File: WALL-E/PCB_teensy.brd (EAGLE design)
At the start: 92.8 x 120.8 mm, 43 parts, among them U4 R-78E5.0-0.5

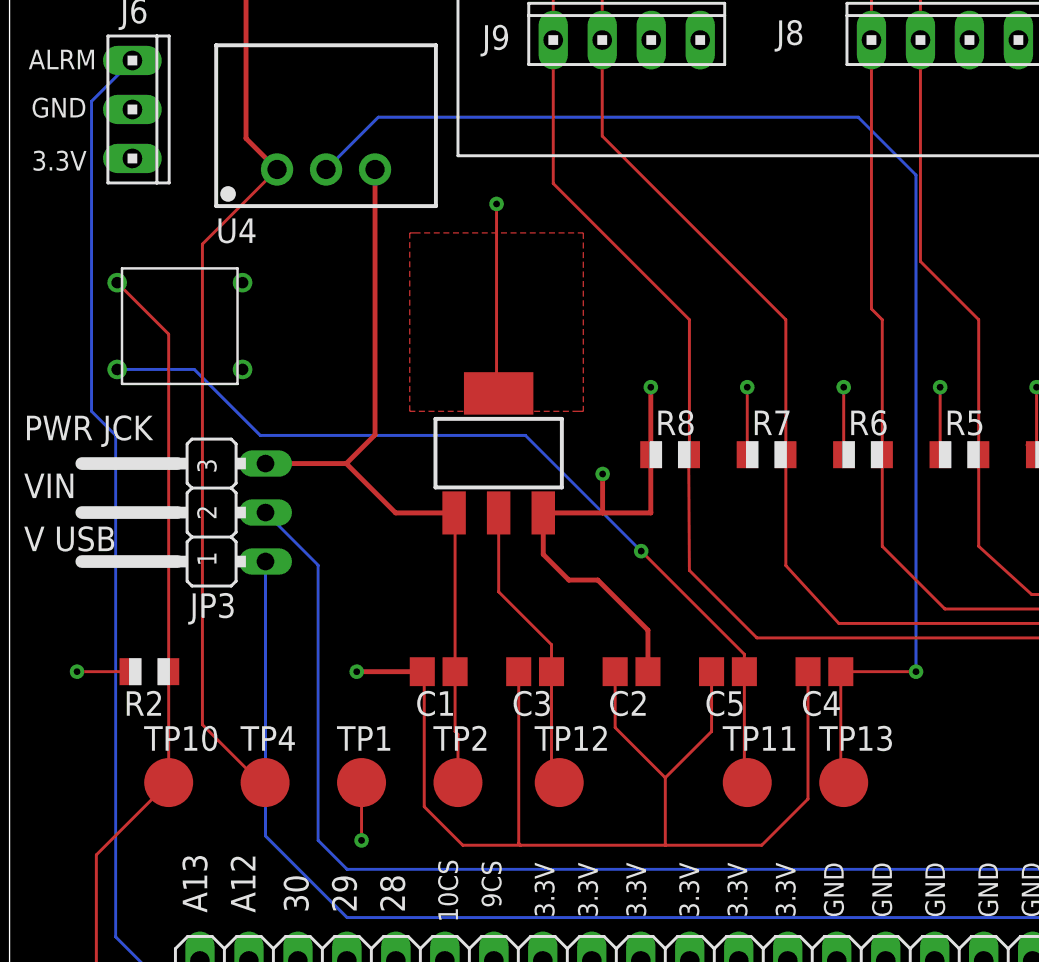
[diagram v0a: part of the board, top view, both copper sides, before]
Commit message: removed some unneeded bypass caps
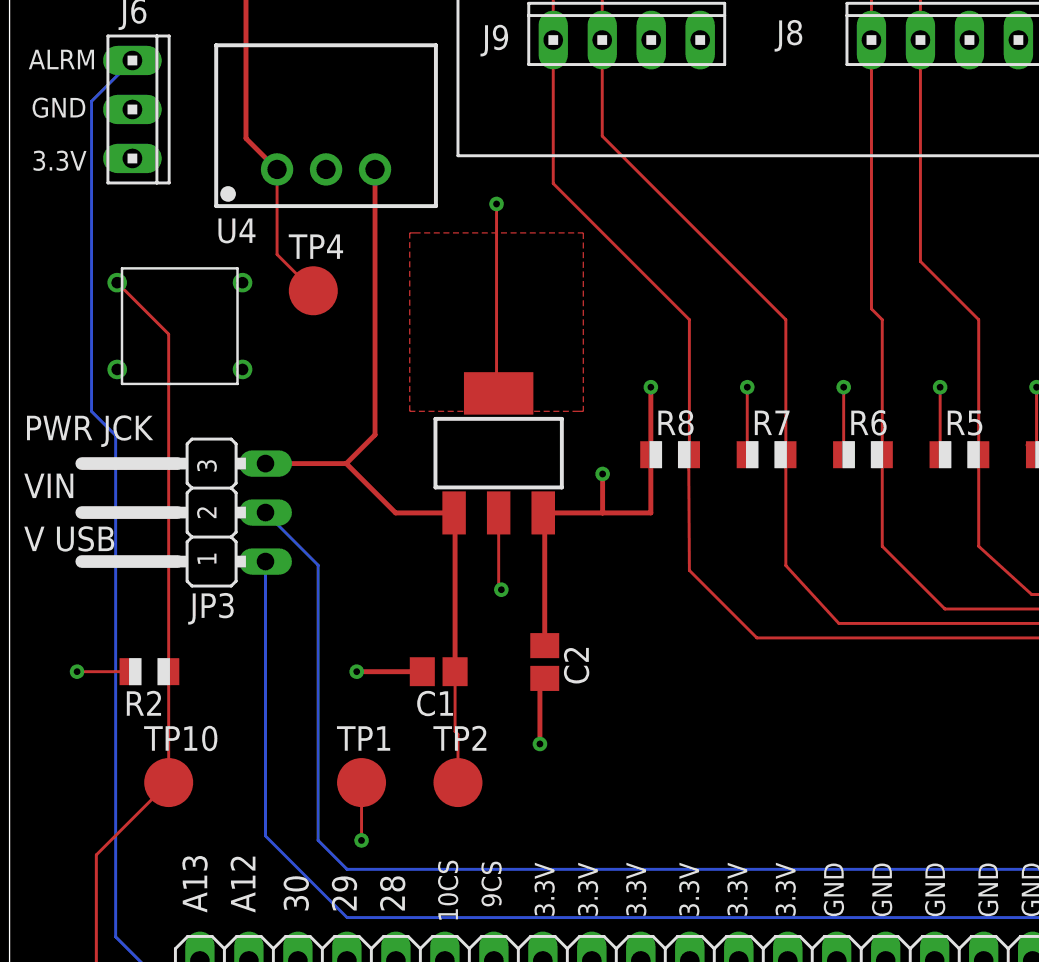
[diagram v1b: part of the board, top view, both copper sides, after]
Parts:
- removed C3, C4, C5: (no value), adafruit:C0805
- removed TP11, TP12, TP13: PTR1B2,54, testpad:B2,54
- moved TP4 25.6 mm to (15.8, 71.0)
- moved C2 4.53 mm to (27.8, 51.8), turned to 270 degrees
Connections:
- removed net N$1: C4.1, TP13.TP, U4.2
- removed net N$3: C3.1, TP12.TP, U$5.2
- removed net N$5: C5.1, TP11.TP, U$2.P$3
- net GND: now also U$2.P$3, U$5.2, U4.2; no longer C3.2, C4.2, C5.2
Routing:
- net N$1: track 68.5 -> 0.00 mm, vias 1 -> 0
- net GND: track 76.2 -> 22.9 mm, vias 3 -> 5
- net N$5: track 45.4 -> 0.00 mm, vias 1 -> 0
- net +12V: track 66.1 -> 38.3 mm
- net N$3: track 15.4 -> 0.00 mm
- net 3.3V: track 49.4 -> 45.0 mm

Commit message: generated new gerber and drill files
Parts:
- moved C1 17.6 mm to (16.2, 67.8)
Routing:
- net 5V: track 40.9 -> 43.0 mm
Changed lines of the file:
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@@
 </autorouter>
 <elements>
-<element name="C1" library="adafruit" library_urn="urn:adsk.eagle:library:420" package="C0805" value="" x="22.25" y="51.25" rot="R180"/>
+<element name="C1" library="adafruit" library_urn="urn:adsk.eagle:library:420" package="C0805" value="" x="16.25" y="67.75" smashed="yes" rot="R180">
+<attribute name="NAME" x="18.139" y="66.234" size="1.27" layer="25" rot="R180"/>
+<attribute name="VALUE" x="17.139" y="70.036" size="1.27" layer="27" rot="R180"/>
+</element>
 <element name="C2" library="adafruit" library_urn="urn:adsk.eagle:library:420" package="C0805" value="" x="27.75" y="51.75" rot="R270"/>
 <element name="J1" library="con-amp" library_urn="urn:adsk.eagle:library:127" package="10X04MTA" value="" x="86.75" y="103.75" smashed="yes" rot="R90">
@@
 <wire x1="25.25" y1="65.789" x2="25.25" y2="75.5" width="0.1524" layer="1"/>
 <via x="25.25" y="75.5" extent="1-16" drill="0.35"/>
-<wire x1="21.5" y1="51.15" x2="21.4" y2="51.25" width="0.1524" layer="1"/>
-<wire x1="21.4" y1="51.25" x2="18" y2="51.25" width="0.254" layer="1"/>
-<via x="18" y="51.25" extent="1-16" drill="0.35"/>
 <wire x1="70.25" y1="8.95" x2="70.25" y2="7" width="0.1524" layer="1"/>
 <via x="70.25" y="7" extent="1-16" drill="0.35"/>
@@
 <wire x1="27.5" y1="50.65" x2="27.5" y2="47.5" width="0.254" layer="1"/>
 <via x="27.5" y="47.5" extent="1-16" drill="0.35"/>
+<wire x1="15.4" y1="67.75" x2="15.4" y2="64.6" width="0.254" layer="1"/>
+<wire x1="15.4" y1="64.6" x2="15.5" y2="64.5" width="0.1524" layer="1"/>
+<via x="15.5" y="64.5" extent="1-16" drill="0.35"/>
 </signal>
 <signal name="5V">
@@
 <wire x1="23" y1="59.4812" x2="23.0486" y2="59.4812" width="0.1524" layer="1"/>
 <wire x1="17.46" y1="62.04" x2="20.0188" y2="59.4812" width="0.254" layer="1"/>
-<wire x1="18.95" y1="77.29" x2="18.95" y2="63.53" width="0.254" layer="1"/>
+<wire x1="18.95" y1="77.29" x2="18.95" y2="67.5" width="0.254" layer="1"/>
+<wire x1="18.95" y1="67.5" x2="18.95" y2="63.53" width="0.254" layer="1"/>
 <wire x1="18.95" y1="63.53" x2="17.46" y2="62.04" width="0.254" layer="1"/>
 <wire x1="23.1" y1="45.65" x2="23.25" y2="45.5" width="0.1524" layer="1"/>
-<wire x1="23.1" y1="51.25" x2="23.1" y2="48.15" width="0.1524" layer="1"/>
-<wire x1="23.1" y1="48.15" x2="23.25" y2="48" width="0.1524" layer="1"/>
 <wire x1="23.25" y1="48" x2="23.25" y2="45.8" width="0.1524" layer="1"/>
 <wire x1="23.25" y1="45.8" x2="23.1" y2="45.65" width="0.1524" layer="1"/>
-<wire x1="23.1" y1="51.25" x2="23.1" y2="59.3812" width="0.254" layer="1"/>
 <wire x1="23.1" y1="59.3812" x2="23" y2="59.4812" width="0.1524" layer="1"/>
+<wire x1="23.0486" y1="59.4812" x2="23.0486" y2="48.2014" width="0.1524" layer="1"/>
+<wire x1="23.0486" y1="48.2014" x2="23.25" y2="48" width="0.1524" layer="1"/>
+<wire x1="18.95" y1="67.5" x2="17.35" y2="67.5" width="0.254" layer="1"/>
+<wire x1="17.35" y1="67.5" x2="17.1" y2="67.75" width="0.1524" layer="1"/>
 </signal>
 <signal name="N$4">

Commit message: fixes power jack and tactile switch
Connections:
- net +12V: now also U$3.TIP, U$6.TIP; no longer TP4.TP, U$3.RING, U$6.RING
- net GND: now also TP4.TP, U$3.RING, U$6.RING; no longer U$3.TIP, U$6.TIP
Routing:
- net GND: track 22.7 -> 29.2 mm
- net +12V: track 38.3 -> 32.4 mm
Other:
- board text added: "Karli Yokotake"
- board text added: "Karthik Kribakaran"
- board text added: "Veena Chandran"
- board text added: "Vincent Wang"
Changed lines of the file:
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@@
 <?xml version="1.0" encoding="utf-8"?>
 <!DOCTYPE eagle SYSTEM "eagle.dtd">
-<eagle version="8.6.3">
+<eagle version="9.0.0">
 <drawing>
 <settings>
@@
 <hole x="5" y="116" drill="3.45"/>
 <hole x="87" y="116" drill="3.45"/>
+<text x="63.5" y="3" size="1.016" layer="21">Karli Yokotake</text>
+<text x="74.5" y="1.5" size="1.016" layer="21">Karthik Kribakaran</text>
+<text x="63.5" y="1.5" size="1.016" layer="21">Vincent Wang</text>
+<text x="74.5" y="3" size="1.016" layer="21">Veena Chandran</text>
 </plain>
 <attributes>
@@
 </elements>
 <signals>
-<signal name="+12V">
-<contactref element="U$6" pad="RING"/>
-<contactref element="U4" pad="1"/>
-<contactref element="U$3" pad="RING"/>
-<contactref element="TP4" pad="TP"/>
-<wire x1="12.26" y1="107.87" x2="12.26" y2="94.69" width="0.254" layer="1"/>
-<wire x1="12.26" y1="94.69" x2="12.26" y2="78.9" width="0.254" layer="1"/>
-<wire x1="12.26" y1="78.9" x2="13.87" y2="77.29" width="0.254" layer="1"/>
-<wire x1="13.87" y1="77.29" x2="13.87" y2="72.88" width="0.1524" layer="1"/>
-<wire x1="13.87" y1="72.88" x2="15.75" y2="71" width="0.1524" layer="1"/>
-</signal>
 <signal name="GND">
-<contactref element="U$6" pad="TIP"/>
-<contactref element="U$6" pad="RING_SW"/>
 <contactref element="U$5" pad="4"/>
 <contactref element="C1" pad="2"/>
@@
 <contactref element="U$1" pad="GND2"/>
 <contactref element="J6" pad="2"/>
-<contactref element="U$3" pad="TIP"/>
-<contactref element="U$3" pad="RING_SW"/>
 <contactref element="J10" pad="2"/>
 <contactref element="J11" pad="2"/>
@@
 <wire x1="15.4" y1="64.6" x2="15.5" y2="64.5" width="0.1524" layer="1"/>
 <via x="15.5" y="64.5" extent="1-16" drill="0.35"/>
+<contactref element="U$3" pad="RING"/>
+<contactref element="TP4" pad="TP"/>
+<contactref element="U$3" pad="RING_SW"/>
+<contactref element="U$6" pad="RING"/>
+<contactref element="U$6" pad="RING_SW"/>
+<wire x1="16.41" y1="77.29" x2="16.41" y2="71.66" width="0.1524" layer="1"/>
+<wire x1="16.41" y1="71.66" x2="15.75" y2="71" width="0.1524" layer="1"/>
 </signal>
 <signal name="5V">
@@
 <wire x1="16" y1="56.77" x2="13.27" y2="59.5" width="0.1524" layer="16"/>
 </signal>
+<signal name="+12V">
+<contactref element="U$3" pad="TIP"/>
+<contactref element="U$6" pad="TIP"/>
+<contactref element="U4" pad="1"/>
+<wire x1="18.16" y1="107.87" x2="18.16" y2="94.69" width="0.1524" layer="1"/>
+<wire x1="18.16" y1="94.69" x2="18.16" y2="81.58" width="0.1524" layer="1"/>
+<wire x1="18.16" y1="81.58" x2="13.87" y2="77.29" width="0.1524" layer="1"/>
+</signal>
 </signals>
